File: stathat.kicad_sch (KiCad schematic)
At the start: 40 parts, among them J1 Raspberry_Pi_2_3, J27 Conn_01x01, J28 Conn_01x01, J29 Conn_01x01, J31 Conn_01x01, J32 Conn_01x01, U26 HCPL3700, U27 HCPL3700, U28 HCPL3700

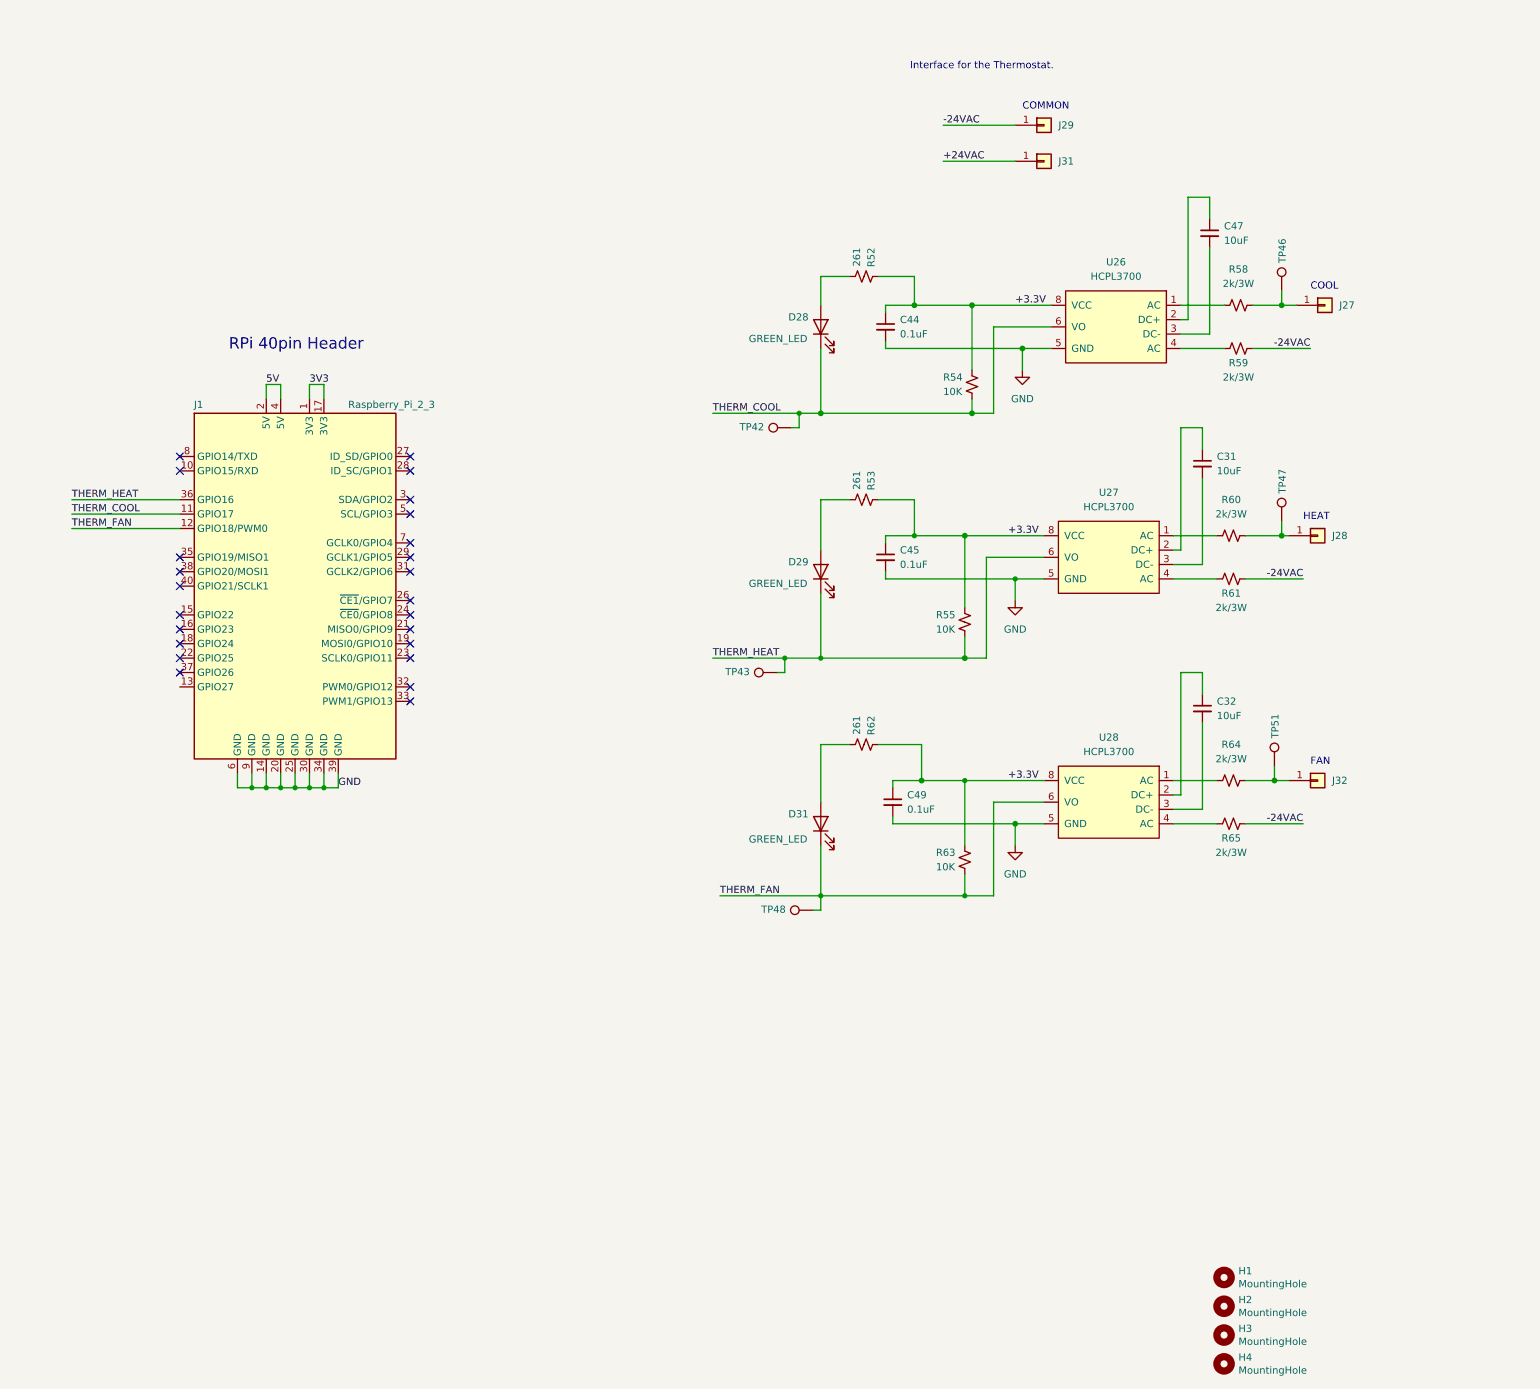
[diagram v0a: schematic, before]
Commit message: fixed schematic. added part numbers. routed PCB
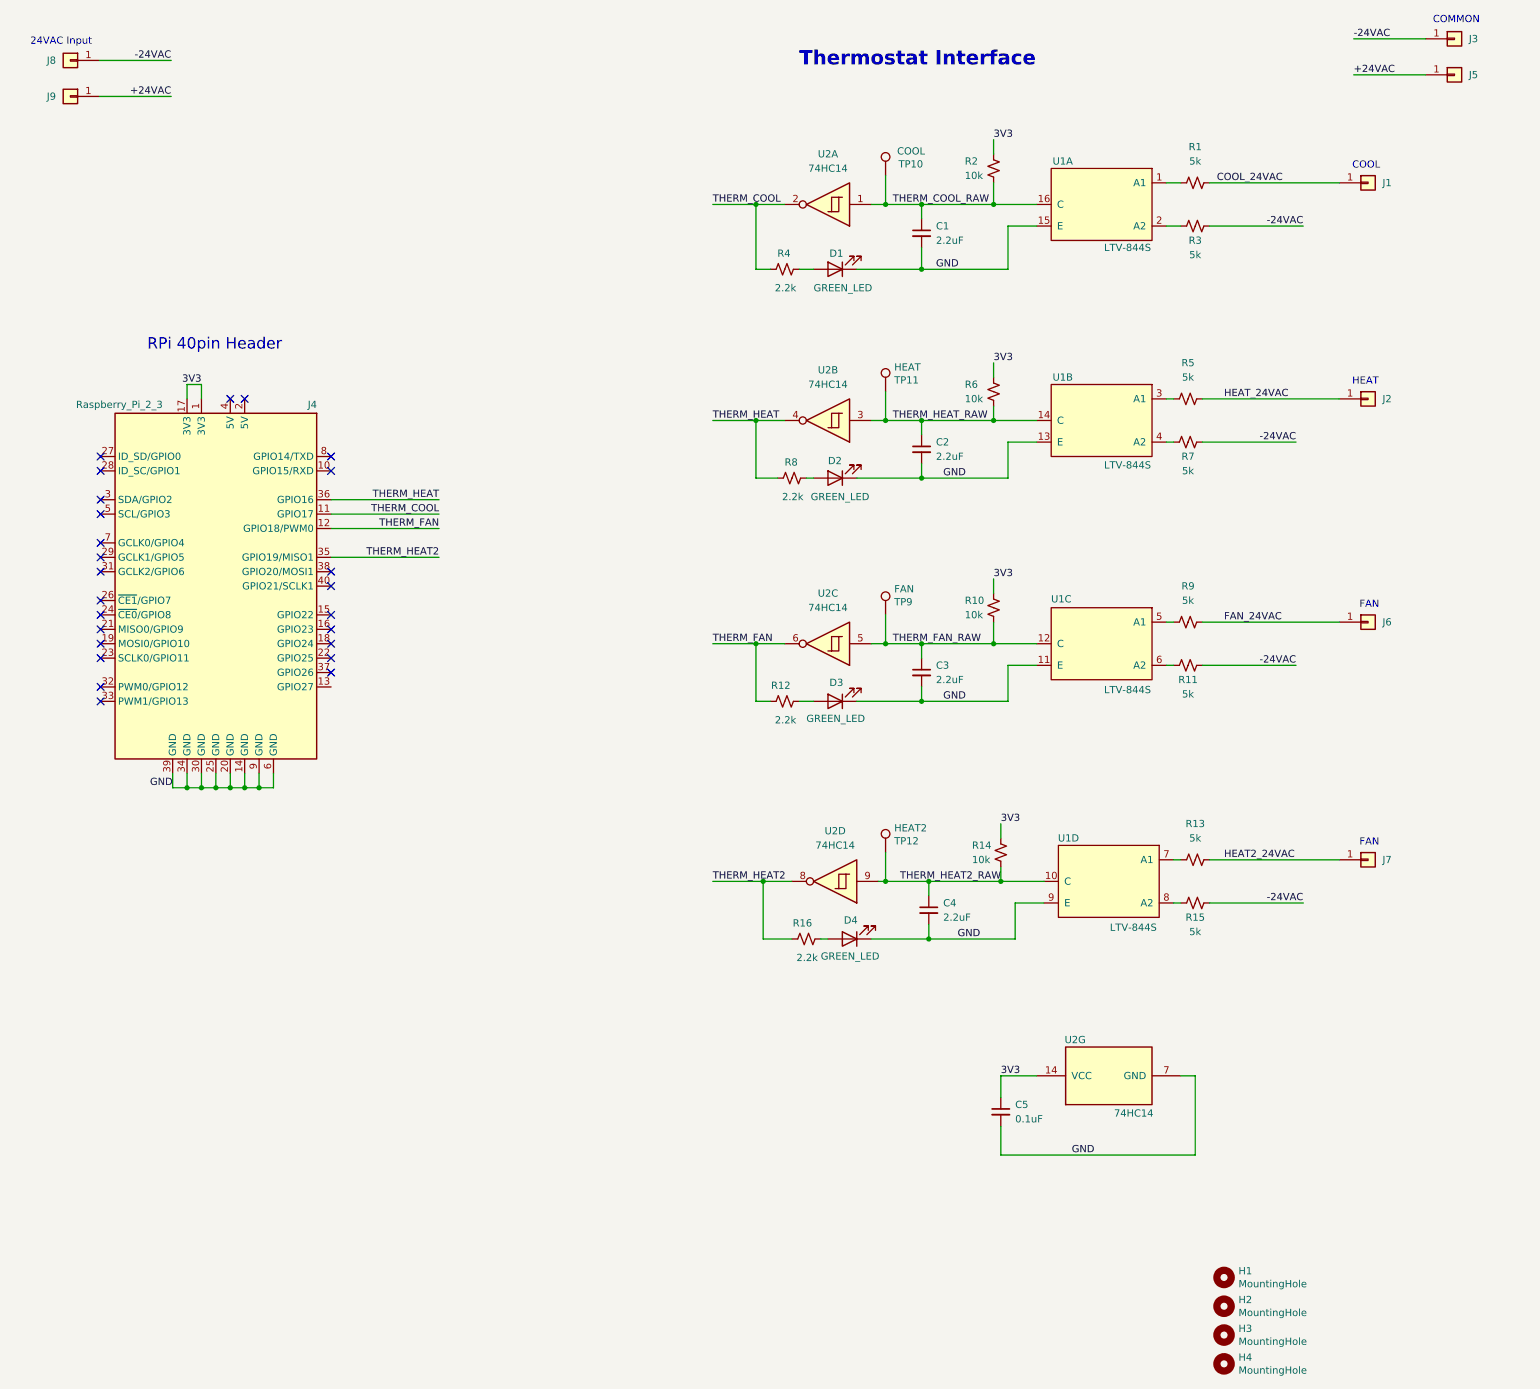
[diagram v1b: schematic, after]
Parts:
- removed C31, C32, C47: 10uF, Resistor_SMD:R_1206_3216Metric, symbol Device:C_Small
- removed R52, R62: 261, Resistor_SMD:R_0402_1005Metric, symbol Device:R_Small_US
- removed TP42, TP43, TP46, TP47, TP48, TP51: TestPoint, TestPoint:TestPoint_Pad_D2.0mm, symbol Connector:TestPoint
- added C4: 2.2uF, Capacitor_SMD:C_0402_1005Metric, symbol Device:C_Small
- added C5: 0.1uF, Capacitor_SMD:C_0402_1005Metric, symbol Device:C_Small
- added D4: GREEN_LED, LED_SMD:LED_0402_1005Metric, symbol Device:LED
- added J7, J8, J9: Conn_01x01, stathat:63862-1, symbol Connector_Generic:Conn_01x01
- added R12, R16, R4: 2.2k, Resistor_SMD:R_0402_1005Metric, symbol Device:R_Small_US
- added R13, R15: 5k, Resistor_SMD:R_1210_3225Metric, symbol Device:R_Small_US
- added R14: 10k, Resistor_SMD:R_0402_1005Metric, symbol Device:R_Small_US
- added TP10: COOL, stathat:TestPoint_Pad_D1.0mm, symbol Connector:TestPoint
- added TP11: HEAT, stathat:TestPoint_Pad_D1.0mm, symbol Connector:TestPoint
- added TP12: HEAT2, stathat:TestPoint_Pad_D1.0mm, symbol Connector:TestPoint
- added TP9: FAN, stathat:TestPoint_Pad_D1.0mm, symbol Connector:TestPoint
- added unit 4 of U1
- added U2: 74HC14, Package_SO:SOIC-14_3.9x8.7mm_P1.27mm, symbol 74xx:74HC14
- C1: renamed from C44; value 0.1uF -> 2.2uF; DK 1292-1640-1-ND -> 1276-1040-1-ND; PARTNO 0402X104K250CT -> CL10A225KO8NNNC
- C2: renamed from C45; value 0.1uF -> 2.2uF; DK 1292-1640-1-ND -> 1276-1040-1-ND; PARTNO 0402X104K250CT -> CL10A225KO8NNNC
- C3: renamed from C49; value 0.1uF -> 2.2uF; DK 1292-1640-1-ND -> 1276-1040-1-ND; PARTNO 0402X104K250CT -> CL10A225KO8NNNC
- D2: renamed from D29; Part Description Green 572nm LED Indication - Discrete 2.2V 2-SMD, No Lead -> (none)
- R1: renamed from R58; value 2k/3W -> 5k; footprint Resistor_SMD:R_2512_6332Metric -> Resistor_SMD:R_1210_3225Metric; DK A121205CT-ND -> 13-RC1210FR-075K1LCT-ND; PARTNO 35222K0FT -> RC1210FR-075K1L
- R10: renamed from R63; value 10K -> 10k
- R11: renamed from R65; value 2k/3W -> 5k; footprint Resistor_SMD:R_2512_6332Metric -> Resistor_SMD:R_1210_3225Metric; DK A121205CT-ND -> 13-RC1210FR-075K1LCT-ND; PARTNO 35222K0FT -> RC1210FR-075K1L
- R2: renamed from R54; value 10K -> 10k
- R3: renamed from R59; value 2k/3W -> 5k; footprint Resistor_SMD:R_2512_6332Metric -> Resistor_SMD:R_1210_3225Metric; DK A121205CT-ND -> 13-RC1210FR-075K1LCT-ND; PARTNO 35222K0FT -> RC1210FR-075K1L
- R5: renamed from R60; value 2k/3W -> 5k; footprint Resistor_SMD:R_2512_6332Metric -> Resistor_SMD:R_1210_3225Metric; DK A121205CT-ND -> 13-RC1210FR-075K1LCT-ND; PARTNO 35222K0FT -> RC1210FR-075K1L
- R6: renamed from R55; value 10K -> 10k
- R7: renamed from R61; value 2k/3W -> 5k; footprint Resistor_SMD:R_2512_6332Metric -> Resistor_SMD:R_1210_3225Metric; DK A121205CT-ND -> 13-RC1210FR-075K1LCT-ND; PARTNO 35222K0FT -> RC1210FR-075K1L
- R8: renamed from R53; value 261 -> 2.2k; DK 541-261LCT-ND -> 311-2.20KLRCT-ND; PARTNO CRCW0402261RFKED -> RC0402FR-072K2L
- R9: renamed from R64; value 2k/3W -> 5k; footprint Resistor_SMD:R_2512_6332Metric -> Resistor_SMD:R_1210_3225Metric; DK A121205CT-ND -> 13-RC1210FR-075K1LCT-ND; PARTNO 35222K0FT -> RC1210FR-075K1L
- U1: renamed from U27; value HCPL3700 -> LTV-844S; footprint stathat:HCPL3700SV -> Package_SO:SOIC-16W_7.5x10.3mm_P1.27mm; symbol stathat:HCPL3700 -> stathat:LTV-844S; DK 2156-HCPL3700SV-ND -> 160-1349-5-ND; LCSC (none) -> C575506; PARTNO HCPL3700SV -> LTV-844S
- U1: renamed from U28; value HCPL3700 -> LTV-844S; footprint stathat:HCPL3700SV -> Package_SO:SOIC-16W_7.5x10.3mm_P1.27mm; symbol stathat:HCPL3700 -> stathat:LTV-844S; DK 2156-HCPL3700SV-ND -> 160-1349-5-ND; LCSC (none) -> C575506; PARTNO HCPL3700SV -> LTV-844S
- U1: renamed from U26; value HCPL3700 -> LTV-844S; footprint stathat:HCPL3700SV -> Package_SO:SOIC-16W_7.5x10.3mm_P1.27mm; symbol stathat:HCPL3700 -> stathat:LTV-844S; DK 2156-HCPL3700SV-ND -> 160-1349-5-ND; LCSC (none) -> C575506; PARTNO HCPL3700SV -> LTV-844S
- renumbered D28 to D1, D31 to D3, J27 to J1, J28 to J2, J29 to J3, J1 to J4, J31 to J5, J32 to J6
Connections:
- net +24VAC: now also J9.1 (Pin_1)
- net -24VAC: now also J8.1 (Pin_1), R15.1
- net 3V3: now also R10.2, R2.2, R6.2, C5.1, R14.2, U2.14 (VCC)
- net GND: now also D1.1 (K), D2.1 (K), D3.1 (K), U1.11 (E), U1.13 (E), U1.15 (E), C4.2, C5.2, D4.1 (K), U1.9 (E), U2.7 (GND); no longer U1.5 (GND), U1.5 (GND), U1.5 (GND)
- net THERM_COOL: now also R4.2, U2.2; no longer D1.1 (K), R2.1, U1.6 (VO)
- net THERM_FAN: now also R12.2, U2.6; no longer D3.1 (K), R10.1, U1.6 (VO)
- net THERM_HEAT: now also R8.2, U2.4; no longer D2.1 (K), R6.1, U1.6 (VO)
- net HEAT_24VAC: now reaches J2.1 (Pin_1), R5.1
- net at R5.2: now also U1.3 (A1); no longer U1.1 (AC)
- net at U1.2 (A2): now also R3.1
- net at R11.2: now also U1.6 (A2); no longer U1.4 (AC)
- net FAN_24VAC: now reaches J6.1 (Pin_1), R9.1
- net at R9.2: now also U1.5 (A1); no longer U1.1 (AC)
- net at D1.2 (A): now also R4.1
- net THERM_HEAT2: now reaches J4.35 (GPIO19/MISO1)
- net THERM_HEAT2: now also R16.2, U2.8
- net at D3.2 (A): now also R12.1
- net COOL_24VAC: now reaches J1.1 (Pin_1), R1.1
- removed net +3.3V: C1.1, C2.1, C3.1, R10.2, R2.2, R6.2, R8.2, U1.8 (VCC), U1.8 (VCC), U1.8 (VCC)
- net 5V: no longer names the net of J4.2 (5V)
- net 5V: no longer J4.4 (5V)
- new net: D4.2 (A), R16.1
- new net: R15.2, U1.8 (A2)
- new net: R13.2, U1.7 (A1)
- new net HEAT2_24VAC: J7.1 (Pin_1), R13.1
- new net THERM_COOL_RAW: C1.1, R2.1, TP10.1, U1.16 (C), U2.1
- new net THERM_FAN_RAW: C3.1, R10.1, TP9.1, U1.12 (C), U2.5
- new net THERM_HEAT2_RAW: C4.1, R14.1, TP12.1, U1.10 (C), U2.9
- new net THERM_HEAT_RAW: C2.1, R6.1, TP11.1, U1.14 (C), U2.3
- no-connect marks 24 -> 25
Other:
- note added: "24VAC Input"
- note added: "Thermostat Interface"
- note removed: "Interface for the Thermostat."
- moved on the sheet: C1, C2, C3, D1, D2, D3, J1, J2, J3, J4, J5, J6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

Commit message: minor DRC and ERC cleanup. updated render
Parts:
- D1, D2, D3, D4: symbol Device:LED -> Device:LED_Filled
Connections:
- no-connect marks 25 -> 26
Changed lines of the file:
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@@
 	(text "24VAC Input"
 		(exclude_from_sim no)
-		(at 79.756 41.91 0)
+		(at 80.01 41.91 0)
 		(effects
 			(font
@@
 	)
 	(no_connect
+		(at 121.92 154.94)
+	)
+	(no_connect
 		(at 121.92 116.84)
 	)
@@
 	(wire
 		(pts
-			(xy 93.726 50.8) (xy 81.026 50.8)
+			(xy 93.98 50.8) (xy 81.28 50.8)
 		)
 		(stroke
@@
 	(wire
 		(pts
-			(xy 93.726 44.45) (xy 81.026 44.45)
+			(xy 93.98 44.45) (xy 81.28 44.45)
 		)
 		(stroke
@@
 	)
 	(label "-24VAC"
-		(at 93.726 44.45 180)
+		(at 93.98 44.45 180)
 		(effects
 			(font
@@
 	)
 	(label "+24VAC"
-		(at 93.726 50.8 180)
+		(at 93.98 50.8 180)
 		(effects
 			(font
@@
 			)
 		)
-		(property "Description" ""
+		(property "Description" "Mounting Hole without connection"
 			(at 279.4 264.16 0)
 			(hide yes)
@@
 	(symbol
 		(lib_id "Connector_Generic:Conn_01x01")
-		(at 75.946 50.8 0)
+		(at 76.2 50.8 0)
 		(mirror y)
 		(unit 1)
@@
 		(dnp no)
 		(property "Reference" "J9"
-			(at 73.406 50.7999 0)
+			(at 73.66 50.7999 0)
 			(show_name no)
 			(do_not_autoplace no)
@@
 		)
 		(property "Value" "Conn_01x01"
-			(at 73.406 52.0699 0)
+			(at 73.66 52.0699 0)
 			(hide yes)
 			(show_name no)
@@
 		)
 		(property "Footprint" "stathat:63862-1"
-			(at 75.946 50.8 0)
+			(at 76.2 50.8 0)
 			(hide yes)
 			(show_name no)
@@
 		)
 		(property "Datasheet" "https://www.te.com/commerce/DocumentDelivery/DDEController?Action=srchrtrv&DocNm=63862&DocType=Customer+Drawing&DocLang=English"
-			(at 75.946 50.8 0)
+			(at 76.2 50.8 0)
 			(hide yes)
 			(show_name no)
@@
 		)
 		(property "Description" ""
-			(at 75.946 50.8 0)
+			(at 76.2 50.8 0)
 			(show_name no)
 			(do_not_autoplace no)
@@
 		)
 		(property "DK" "A100886CT-ND"
-			(at 75.946 50.8 0)
+			(at 76.2 50.8 0)
 			(hide yes)
 			(show_name no)
@@
 		)
 		(property "PARTNO" "63862-1"
-			(at 75.946 50.8 0)
+			(at 76.2 50.8 0)
 			(hide yes)
 			(show_name no)
@@
 		)
 		(property "DNP" ""
-			(at 75.946 50.8 0)
+			(at 76.2 50.8 0)
 			(hide yes)
 			(show_name no)
@@
 	(symbol
 		(lib_id "Connector_Generic:Conn_01x01")
-		(at 75.946 44.45 0)
+		(at 76.2 44.45 0)
 		(mirror y)
 		(unit 1)
@@
 		(dnp no)
 		(property "Reference" "J8"
-			(at 73.406 44.4499 0)
+			(at 73.66 44.4499 0)
 			(show_name no)
 			(do_not_autoplace no)
@@
 		)
 		(property "Value" "Conn_01x01"
-			(at 73.406 45.7199 0)
+			(at 73.66 45.7199 0)
 			(hide yes)
 			(show_name no)
@@
 		)
 		(property "Footprint" "stathat:63862-1"
-			(at 75.946 44.45 0)
+			(at 76.2 44.45 0)
 			(hide yes)
 			(show_name no)
@@
 		)
 		(property "Datasheet" "https://www.te.com/commerce/DocumentDelivery/DDEController?Action=srchrtrv&DocNm=63862&DocType=Customer+Drawing&DocLang=English"
-			(at 75.946 44.45 0)
+			(at 76.2 44.45 0)
 			(hide yes)
 			(show_name no)
@@
 		)
 		(property "Description" ""
-			(at 75.946 44.45 0)
+			(at 76.2 44.45 0)
 			(show_name no)
 			(do_not_autoplace no)
@@
 		)
 		(property "DK" "A100886CT-ND"
-			(at 75.946 44.45 0)
+			(at 76.2 44.45 0)
 			(hide yes)
 			(show_name no)
@@
 		)
 		(property "PARTNO" "63862-1"
-			(at 75.946 44.45 0)
+			(at 76.2 44.45 0)
 			(hide yes)
 			(show_name no)
@@
 		)
 		(property "DNP" ""
-			(at 75.946 44.45 0)
+			(at 76.2 44.45 0)
 			(hide yes)
 			(show_name no)
@@
 			)
 		)
-		(property "Description" ""
+		(property "Description" "Mounting Hole without connection"
 			(at 279.4 259.08 0)
 			(hide yes)
@@
 	)
 	(symbol
-		(lib_id "Device:LED")
+		(lib_id "Device:LED_Filled")
 		(at 210.82 81.28 180)
 		(unit 1)
@@
 			)
 		)
-		(property "Description" ""
+		(property "Description" "Light emitting diode, filled shape"
 			(at 210.82 81.28 0)
+			(hide yes)
 			(show_name no)
 			(do_not_autoplace no)
@@
 			)
 		)
+		(property "Sim.Pins" "1=K 2=A"
+			(at 210.82 81.28 0)
+			(hide yes)
+			(show_name no)
+			(do_not_autoplace no)
+			(effects
+				(font
+					(size 1.27 1.27)
+				)
+			)
+		)
 		(pin "1"
 		)
@@
 			)
 		)
-		(property "Description" ""
+		(property "Description" "Mounting Hole without connection"
 			(at 279.4 269.24 0)
 			(hide yes)
@@
 	)
 	(symbol
-		(lib_id "Device:LED")
+		(lib_id "Device:LED_Filled")
 		(at 210.82 118.11 180)
 		(unit 1)
@@
 			)
 		)
-		(property "Description" ""
+		(property "Description" "Light emitting diode, filled shape"
 			(at 210.82 118.11 0)
+			(hide yes)
 			(show_name no)
 			(do_not_autoplace no)
@@
 			)
 		)
+		(property "Sim.Pins" "1=K 2=A"
+			(at 210.82 118.11 0)
+			(hide yes)
+			(show_name no)
+			(do_not_autoplace no)
+			(effects
+				(font
+					(size 1.27 1.27)
+				)
+			)
+		)
 		(pin "1"
 		)
@@
 	)
 	(symbol
-		(lib_id "Device:LED")
+		(lib_id "Device:LED_Filled")
 		(at 213.36 199.39 180)
 		(unit 1)
@@
 			)
 		)
-		(property "Description" ""
+		(property "Description" "Light emitting diode, filled shape"
 			(at 213.36 199.39 0)
+			(hide yes)
 			(show_name no)
 			(do_not_autoplace no)
@@
 			)
 		)
+		(property "Sim.Pins" "1=K 2=A"
+			(at 213.36 199.39 0)
+			(hide yes)
+			(show_name no)
+			(do_not_autoplace no)
+			(effects
+				(font
+					(size 1.27 1.27)
+				)
+			)
+		)
 		(pin "1"
 		)
@@
 	)
 	(symbol
-		(lib_id "Device:LED")
+		(lib_id "Device:LED_Filled")
 		(at 210.82 157.48 180)
 		(unit 1)
@@
 			)
 		)
-		(property "Description" ""
+		(property "Description" "Light emitting diode, filled shape"
 			(at 210.82 157.48 0)
+			(hide yes)
 			(show_name no)
 			(do_not_autoplace no)
@@
 			)
 		)
+		(property "Sim.Pins" "1=K 2=A"
+			(at 210.82 157.48 0)
+			(hide yes)
+			(show_name no)
+			(do_not_autoplace no)
+			(effects
+				(font
+					(size 1.27 1.27)
+				)
+			)
+		)
 		(pin "1"
 		)
@@
 			)
 		)
-		(property "Description" ""
+		(property "Description" "Mounting Hole without connection"
 			(at 279.4 274.32 0)
 			(hide yes)
